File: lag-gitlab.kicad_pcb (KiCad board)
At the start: 2 copper layers, 0 parts

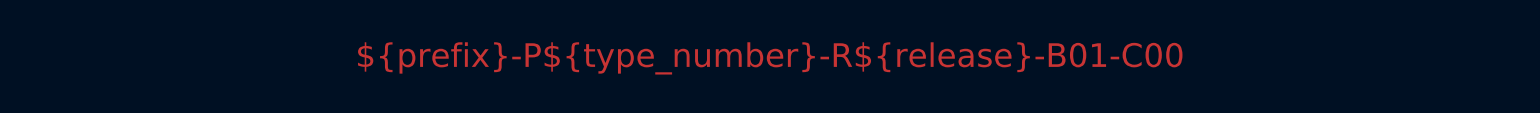
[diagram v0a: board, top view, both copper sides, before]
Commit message: Add more fields, add some info-text to sch and pcb
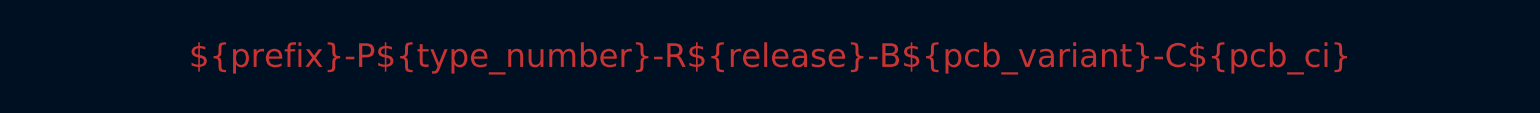
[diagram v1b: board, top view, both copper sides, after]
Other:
- board text added: "${prefix}-P${type_number}-R${release}-B${pcb_variant}-C${pcb_ci}"
- board text added: "Steps to complete setting up this PCB: * Update the PCB Layerstack * Check electrical rules * Setup minimal / default track width"
- board text removed: "${prefix}-P${type_number}-R${release}-B01-C00"
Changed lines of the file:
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@@
     (company "${company}")
     (comment 1 "${release_state}")
-    (comment 2 "${prefix}-P${type_number}-R${release}-B01-C00")
+    (comment 2 "${prefix}-P${type_number}-R${release}-B${pcb_variant}-C${pcb_ci}")
     (comment 3 "hardware/${prefix}-S${type_number}_${short_desciption}")
   )
@@
     (48 "B.Fab" user)
     (49 "F.Fab" user)
-    (50 "User.1" user)
-    (51 "User.2" user)
-    (52 "User.3" user)
-    (53 "User.4" user)
-    (54 "User.5" user)
-    (55 "User.6" user)
-    (56 "User.7" user)
-    (57 "User.8" user)
-    (58 "User.9" user)
+    (50 "User.1" user "Nutzer.1")
+    (51 "User.2" user "Nutzer.2")
+    (52 "User.3" user "Nutzer.3")
+    (53 "User.4" user "Nutzer.4")
+    (54 "User.5" user "Nutzer.5")
+    (55 "User.6" user "Nutzer.6")
+    (56 "User.7" user "Nutzer.7")
+    (57 "User.8" user "Nutzer.8")
+    (58 "User.9" user "Nutzer.9")
   )
   (setup
+    (stackup
+      (layer "F.SilkS" (type "Top Silk Screen"))
+      (layer "F.Paste" (type "Top Solder Paste"))
+      (layer "F.Mask" (type "Top Solder Mask") (thickness 0.01))
+      (layer "F.Cu" (type "copper") (thickness 0.035))
+      (layer "dielectric 1" (type "core") (thickness 1.51) (material "FR4") (epsilon_r 4.5) (loss_tangent 0.02))
+      (layer "B.Cu" (type "copper") (thickness 0.035))
+      (layer "B.Mask" (type "Bottom Solder Mask") (thickness 0.01))
+      (layer "B.Paste" (type "Bottom Solder Paste"))
+      (layer "B.SilkS" (type "Bottom Silk Screen"))
+      (copper_finish "None")
+      (dielectric_constraints no)
+    )
     (pad_to_mask_clearance 0)
     (pcbplotparams
@@
   )
   (property "company" "Linux Automation GmbH")
+  (property "pcb_ci" "00")
+  (property "pcb_variant" "01")
   (property "prefix" "template")
   (property "release" "01")
   (property "release_state" "draft")
+  (property "sch_ci" "00")
+  (property "sch_variant" "01")
   (property "short_desciption" "template_for_LAG_projects")
-  (property "title" "Tamplate Project")
+  (property "title" "Template Project")
   (property "type_number" "01")
   (net 0 "")
-  (gr_text "${prefix}-P${type_number}-R${release}-B01-C00" (at 128.5 122.7) (layer "F.Cu")
+  (gr_text "${prefix}-P${type_number}-R${release}-B${pcb_variant}-C${pcb_ci}" (at 128.5 122.7) (layer "F.Cu")
     (effects (font (size 1.5 1.5) (thickness 0.3)))
   )
+  (gr_text "Steps to complete setting up this PCB:\n\n* Update the PCB Layerstack\n* Check electrical rules\n* Setup minimal / default track width" (at 88 97) (layer "Eco1.User")
+    (effects (font (size 3 3) (thickness 0.15)) (justify left))
+  )
 )
